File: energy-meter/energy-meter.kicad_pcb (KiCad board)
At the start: 2 copper layers, 82 x 62.5 mm, 61 parts, among them J1 Screw_Terminal_01x04, J2 Conn_01x03, J3 I2C OLED Display, etc., K1 G5RL-U1A-E, K2 DNP / HF3FF/005-1HST, P1 PineNut, Q11 AP3400, T1 AP-2500, T2 BV 202 0154, T3 DNP / AP-2500, U1 L9110S, U11 SLG47004, U9 GD32VF103

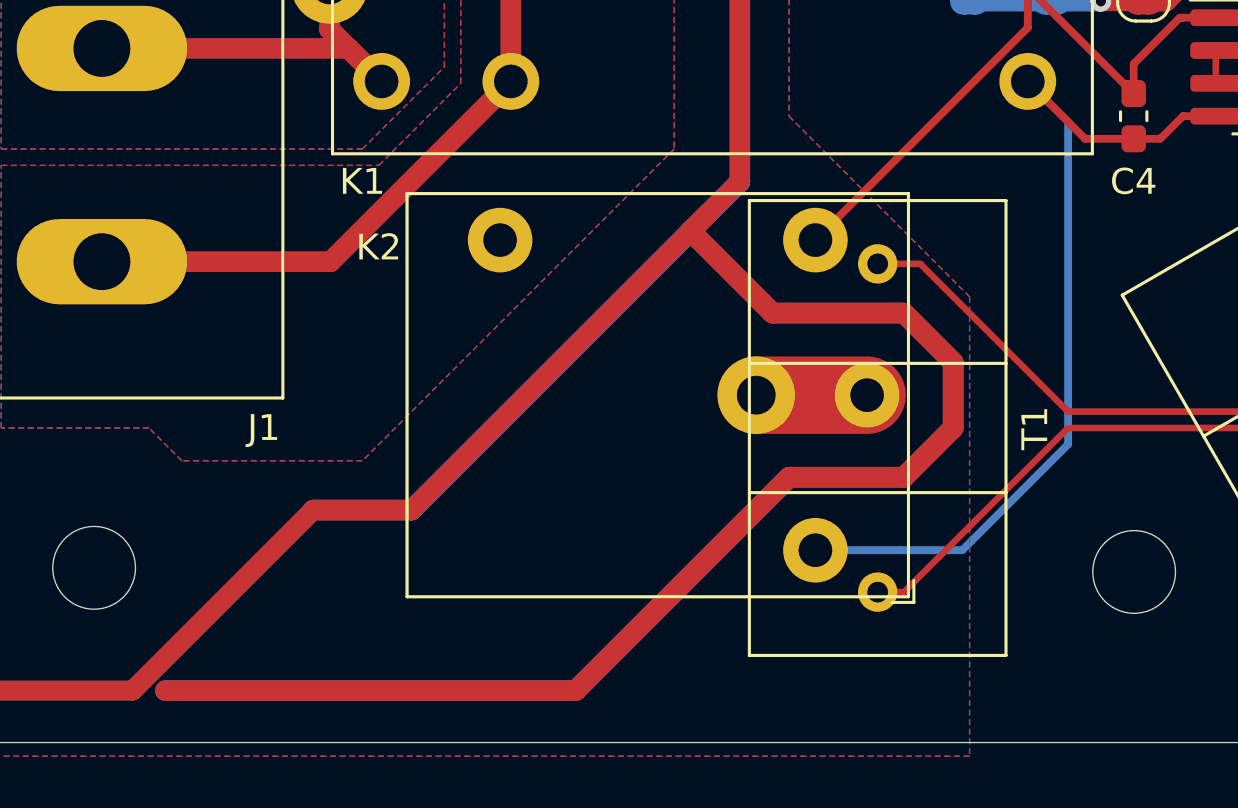
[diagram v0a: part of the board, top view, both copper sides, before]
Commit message: add optional internal load resistor
This may be useful for calibration and tests.
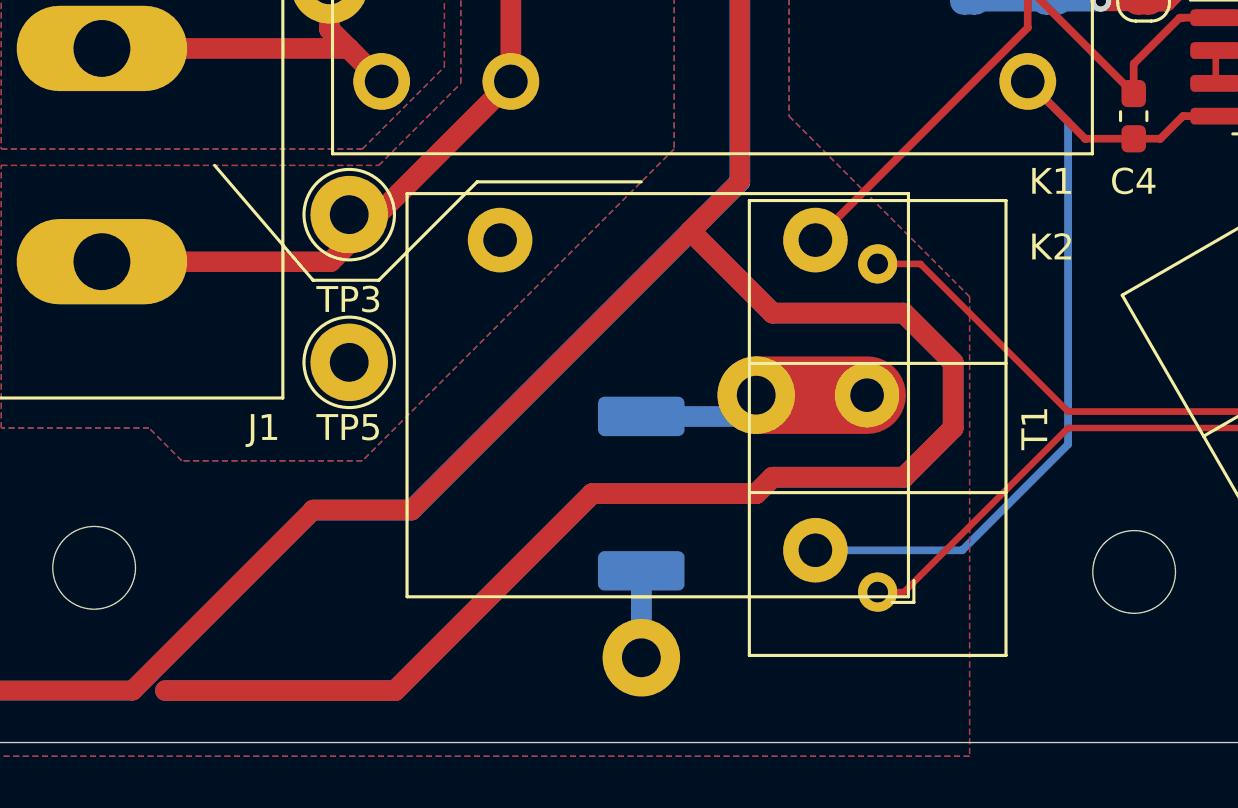
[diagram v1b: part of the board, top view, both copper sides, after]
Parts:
- added R5: 39kOhm, 2W, 1%, Resistor_SMD:R_2512_6332Metric_Pad1.52x3.35mm_HandSolder, B.Cu at (131.6, 146.2)
- added TP3: TestPoint, TestPoint:TestPoint_THTPad_D3.0mm_Drill1.5mm, F.Cu at (120.3, 135.4)
- added TP4: TestPoint, TestPoint:TestPoint_THTPad_D3.0mm_Drill1.5mm, B.Cu at (131.6, 152.6)
- added TP5: TestPoint, TestPoint:TestPoint_THTPad_D3.0mm_Drill1.5mm, F.Cu at (120.3, 141.1)
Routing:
- net Net-(K2-Pad1): track 4.29 -> 9.08 mm
- net Net-(R5-Pad1): track 0.00 -> 3.36 mm

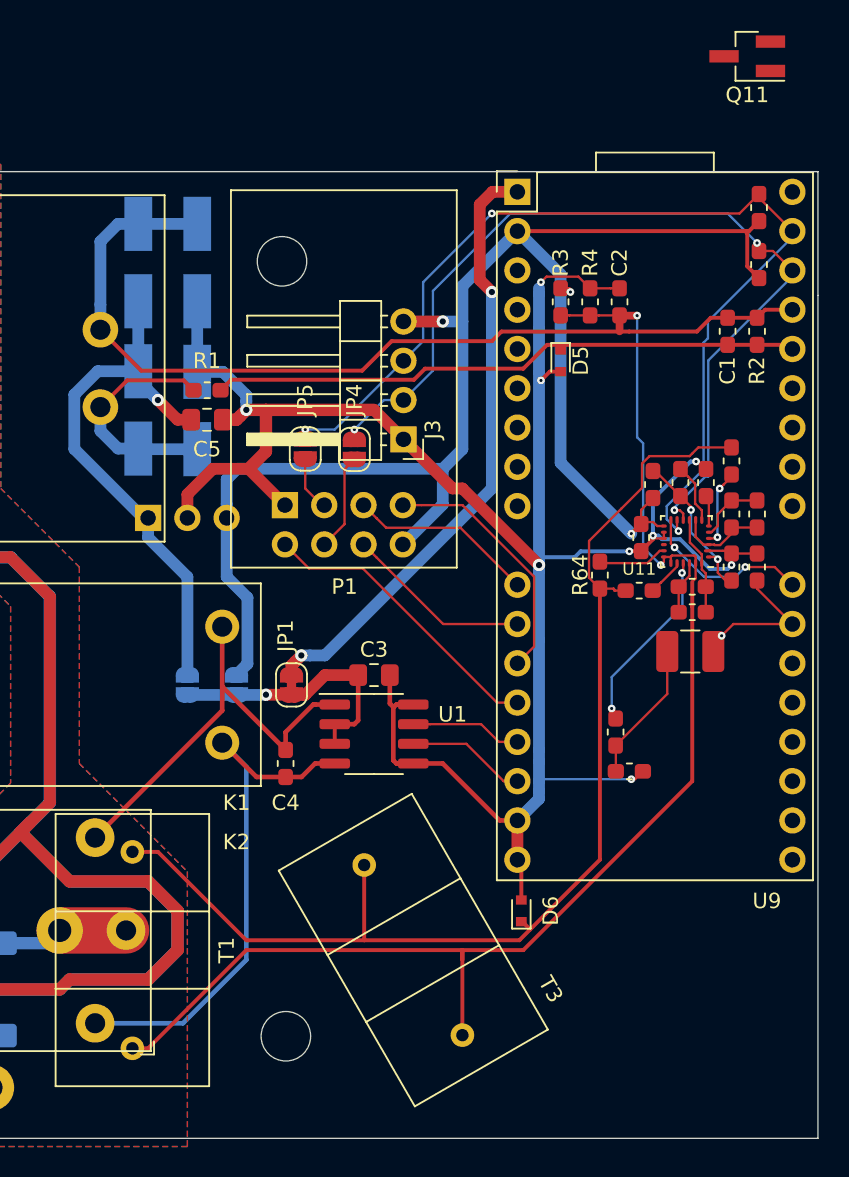
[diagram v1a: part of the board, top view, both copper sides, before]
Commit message: 2nd relay needs an additional driver if we want to use both of them
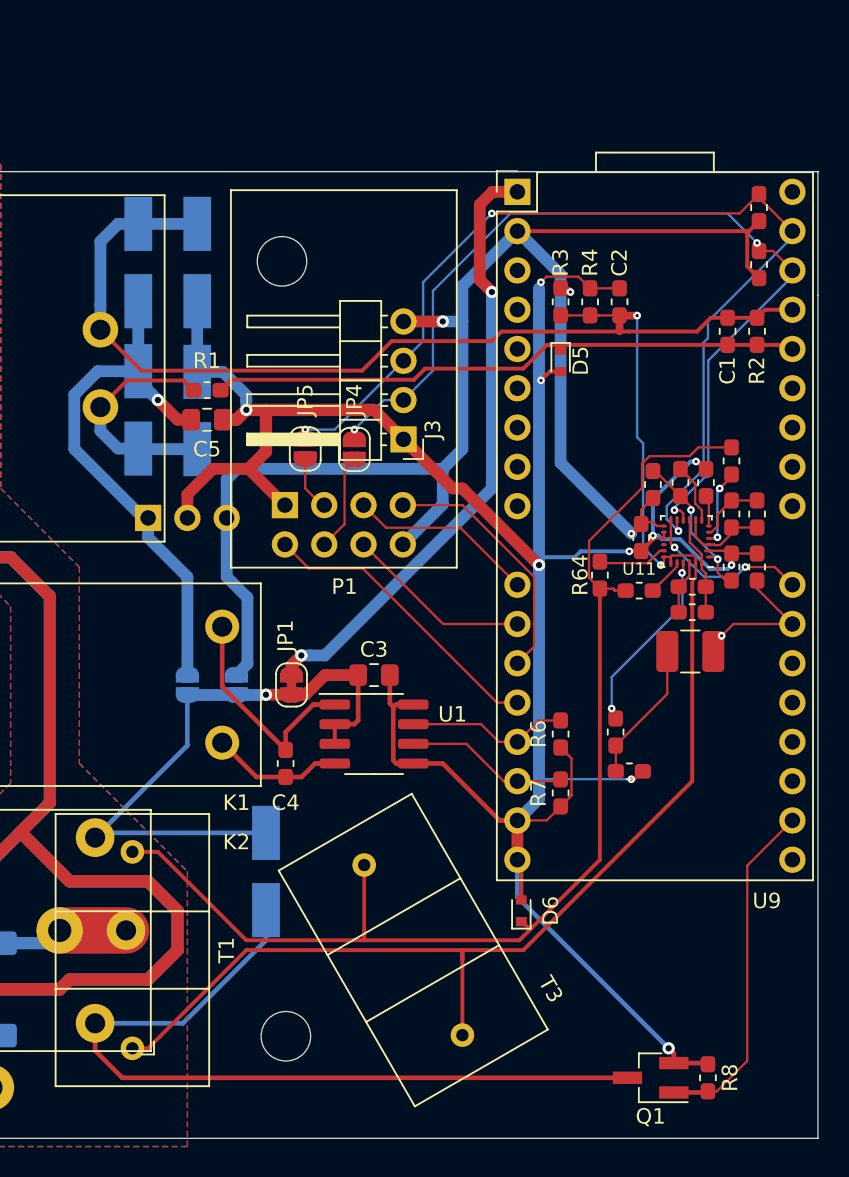
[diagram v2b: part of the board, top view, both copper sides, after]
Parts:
- removed Q11: AP3400, Package_TO_SOT_SMD:SOT-23_Handsoldering
- added D7: D_Schottky, Diode_SMD:D_SMA_Handsoldering, B.Cu at (149.4, 138.6)
- added Q1: AP3400, Package_TO_SOT_SMD:SOT-23_Handsoldering, F.Cu at (174.2, 151.9)
- added R6: 10k, Resistor_SMD:R_0603_1608Metric_Pad1.05x0.95mm_HandSolder, F.Cu at (168.4, 129.7)
- added R7: 10k, Resistor_SMD:R_0603_1608Metric_Pad1.05x0.95mm_HandSolder, F.Cu at (168.4, 133.5)
- added R8: 10k, Resistor_SMD:R_0603_1608Metric_Pad1.05x0.95mm_HandSolder, F.Cu at (178.0, 151.9)
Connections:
- C3 pad 1: Net-(C3-Pad1) -> /VCC_COIL
- JP1 pad 2: Net-(C3-Pad1) -> /VCC_COIL
- JP2 pad 2: Net-(C3-Pad1) -> /VCC_COIL
- JP3 pad 2: Net-(C3-Pad1) -> /VCC_COIL
- K2 pad 2: /coil+ -> /VCC_COIL
- K2 pad 6: /coil- -> Net-(D7-Pad2)
- U1 pad 2: Net-(C3-Pad1) -> /VCC_COIL
- U1 pad 3: Net-(C3-Pad1) -> /VCC_COIL
- U9 pad 20: Net-(U9-Pad20) -> /RELAY2
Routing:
- net Net-(D7-Pad2): track 0.00 -> 52.1 mm
- net /VCC_COIL: track 0.00 -> 40.3 mm, vias 0 -> 1
- net GND: track 148.1 -> 177.8 mm, vias 9 -> 10
- net /coil-: track 34.7 -> 8.56 mm
- net /RELAY2: track 0.00 -> 22.3 mm
- net Net-(C3-Pad1): track 17.4 -> 0.00 mm, vias 1 -> 0
- net /coil+: track 27.9 -> 14.7 mm
- net /RELAY_SET: track 7.21 -> 10.6 mm
- net /RELAY_RESET: track 7.73 -> 10.6 mm

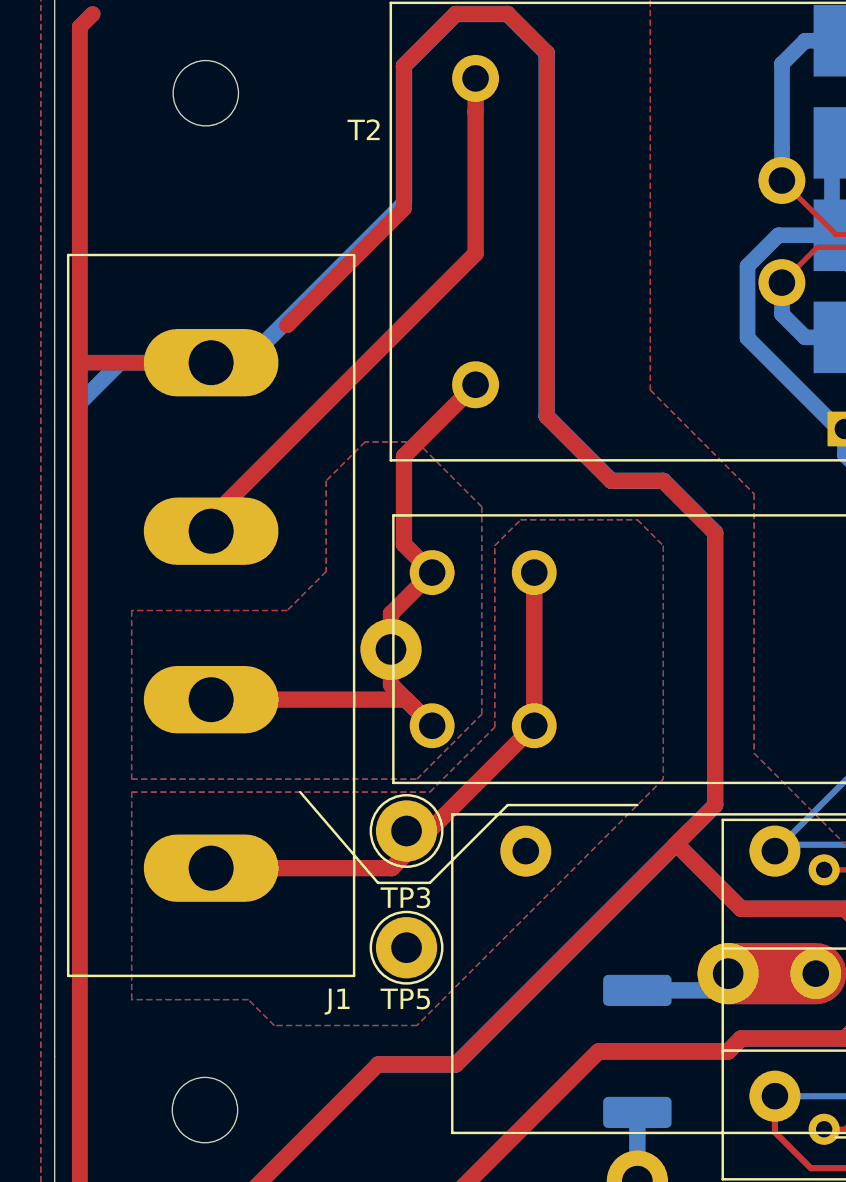
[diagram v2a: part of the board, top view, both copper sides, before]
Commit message: add some vias for PE
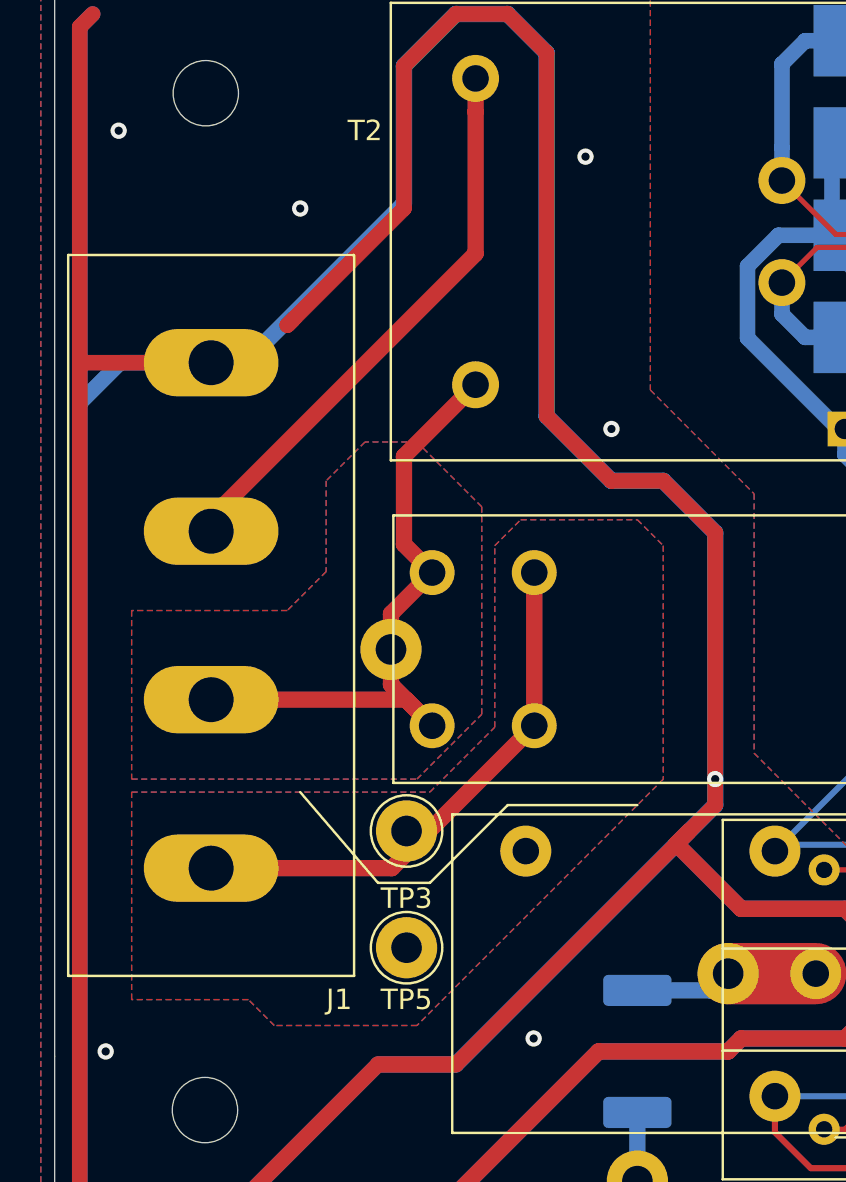
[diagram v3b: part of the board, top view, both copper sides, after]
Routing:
- net PE: vias 0 -> 7
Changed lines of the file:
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@@
     (thickness 1)
     (drawings 44)
-    (tracks 574)
+    (tracks 582)
     (zones 0)
     (modules 69)
@@
   (segment (start 125.25 95.405) (end 127.155 97.31) (width 0.8) (layer B.Cu) (net 39))
   (segment (start 118.9 146.84) (end 122.71 146.84) (width 0.8) (layer F.Cu) (net 39))
-  (segment (start 135.41 134.14) (end 135.41 120.805) (width 0.762) (layer F.Cu) (net 39))
+  (segment (start 135.41 134.14) (end 135.41 132.87) (width 0.762) (layer F.Cu) (net 39))
   (segment (start 135.41 120.805) (end 132.87 118.265) (width 0.762) (layer F.Cu) (net 39))
   (segment (start 132.87 118.265) (end 130.33 118.265) (width 0.762) (layer F.Cu) (net 39))
@@
   (segment (start 133.505 136.045) (end 136.68 139.22) (width 0.8) (layer F.Cu) (net 39))
   (segment (start 143.665 143.665) (end 141.76 145.57) (width 0.8) (layer F.Cu) (net 39))
+  (via (at 129.06 102.39) (size 0.8) (drill 0.4) (layers F.Cu B.Cu) (net 39))
+  (via (at 130.33 115.725) (size 0.8) (drill 0.4) (layers F.Cu B.Cu) (net 39))
+  (segment (start 135.41 132.87) (end 135.41 120.805) (width 0.762) (layer F.Cu) (net 39))
+  (via (at 135.41 132.87) (size 0.8) (drill 0.4) (layers F.Cu B.Cu) (net 39))
+  (via (at 126.52 145.57) (size 0.8) (drill 0.4) (layers F.Cu B.Cu) (net 39))
+  (via (at 105.565 146.205) (size 0.8) (drill 0.4) (layers F.Cu B.Cu) (net 39))
+  (via (at 115.09 104.93) (size 0.8) (drill 0.4) (layers F.Cu B.Cu) (net 39))
+  (via (at 106.2 101.12) (size 0.8) (drill 0.4) (layers F.Cu B.Cu) (net 39))
   (segment (start 144.935 96.715) (end 141.125 96.715) (width 0.762) (layer B.Cu) (net 40))
   (segment (start 138.676 101.932655) (end 138.676 103.559) (width 0.762) (layer B.Cu) (net 40))

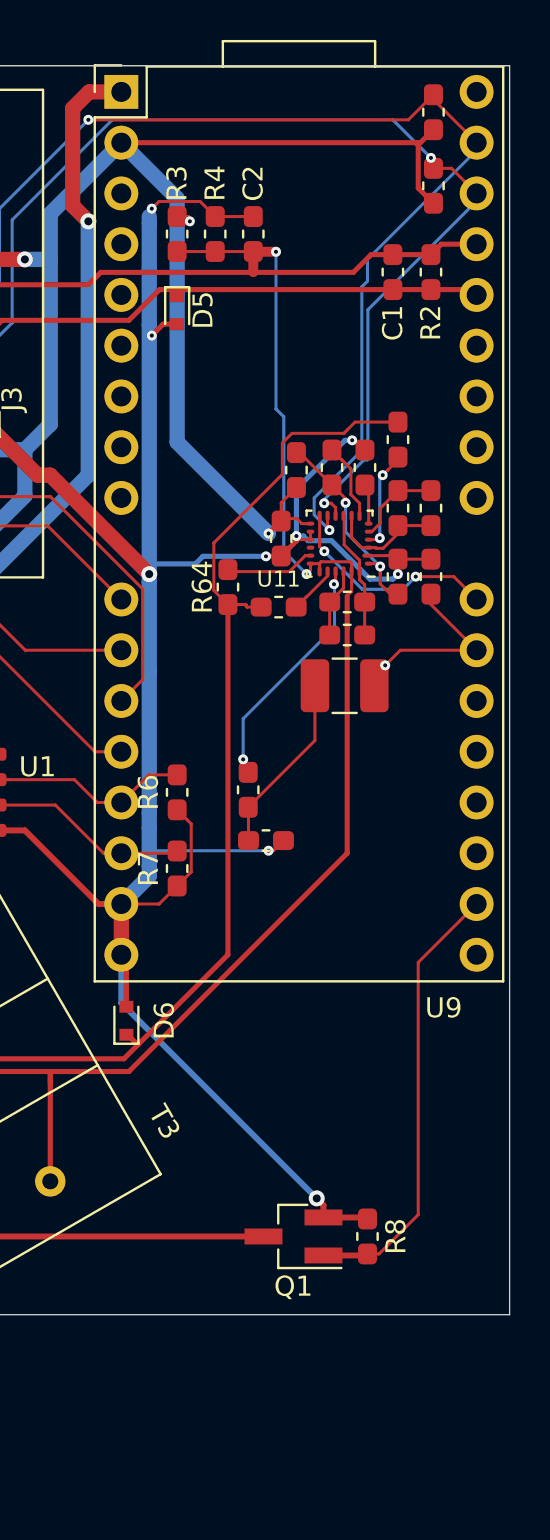
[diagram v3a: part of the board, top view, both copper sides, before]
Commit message: adjust voltage divider to somewhat work if transformer is also used for VCC
In that case, we will only see one half of the wave.
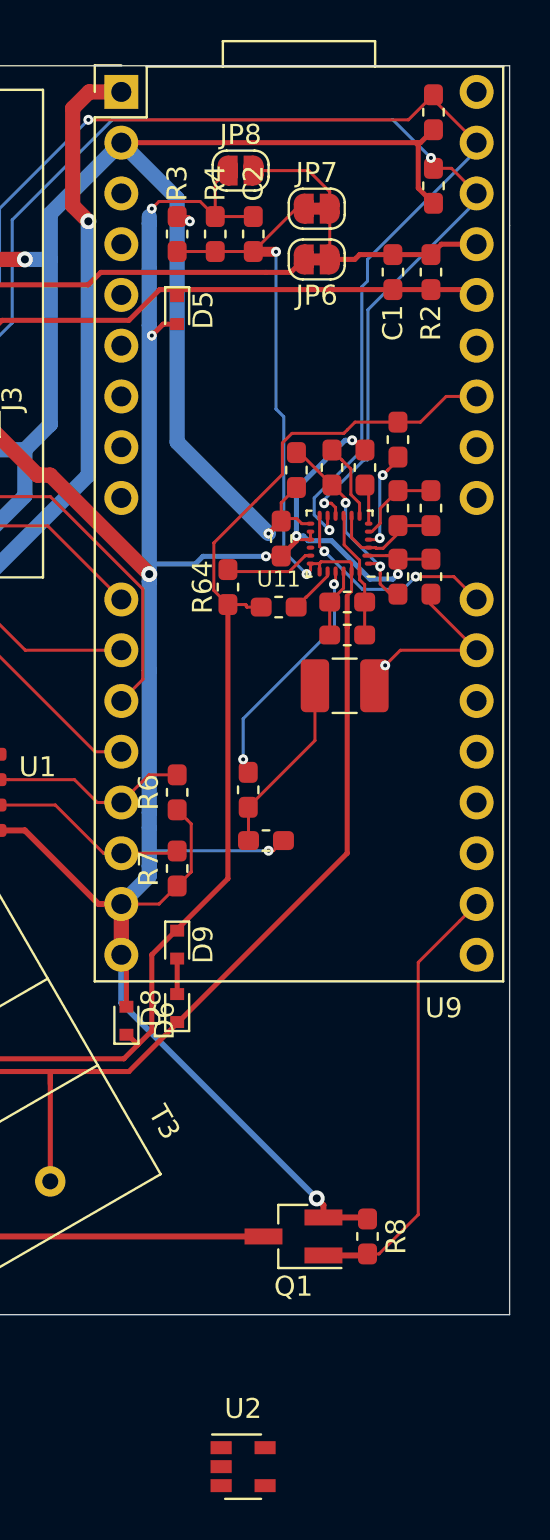
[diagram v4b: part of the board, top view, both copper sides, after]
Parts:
- removed NT1: Net-Tie_2, NetTie:NetTie-2_SMD_Pad0.5mm
- added D8: ESD5Z5.0T1G, Diode_SMD:D_SOD-523, F.Cu at (168.4, 140.5)
- added D9: ESD5Z5.0T1G, Diode_SMD:D_SOD-523, F.Cu at (168.4, 137.3)
- added JP6: SolderJumper_2_Bridged, Jumper:SolderJumper-2_P1.3mm_Bridged_RoundedPad1.0x1.5mm, F.Cu at (175.4, 103.0)
- added JP7: SolderJumper_2_Bridged, Jumper:SolderJumper-2_P1.3mm_Bridged_RoundedPad1.0x1.5mm, F.Cu at (175.4, 100.5)
- added JP8: SolderJumper_2_Open, Jumper:SolderJumper-2_P1.3mm_Open_RoundedPad1.0x1.5mm, F.Cu at (171.6, 98.6)
- added U2: MCP6V96T-E/OT, Package_TO_SOT_SMD:SOT-23-5, F.Cu at (171.7, 163.4)
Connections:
- C1 pad 2: /VOLTAGE1 -> /VOLTAGE1B
- R2 pad 1: /VOLTAGE1 -> /VOLTAGE1B
- U9 pad 30: Net-(U9-Pad30) -> /CURRENT0
- U9 pad 33: /VOLTAGE1 -> /VOLTAGE1B
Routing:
- net /VOLTAGE1B: track 0.00 -> 15.3 mm
- net /VOLTAGE1: track 60.7 -> 51.6 mm
- net /CURRENT0: track 75.7 -> 80.2 mm
- net /BIAS: track 3.81 -> 7.22 mm
- net GND: track 177.8 -> 180.4 mm
- net Net-(D8-Pad2): track 0.00 -> 1.78 mm
